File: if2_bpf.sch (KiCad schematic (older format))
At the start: 16 parts

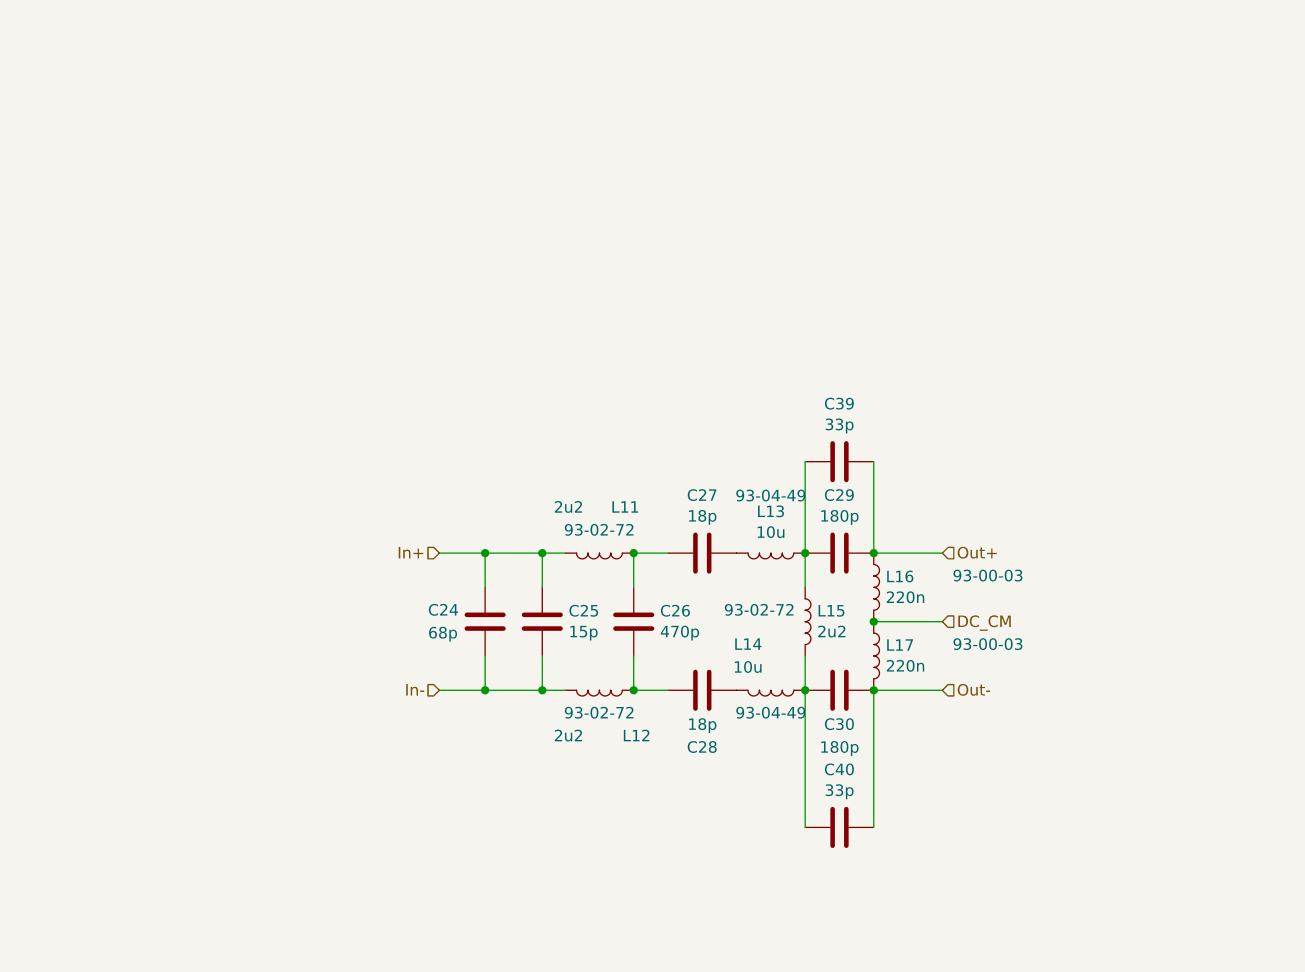
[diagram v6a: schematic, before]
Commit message: if2_bpf revised + Schematic cleanup
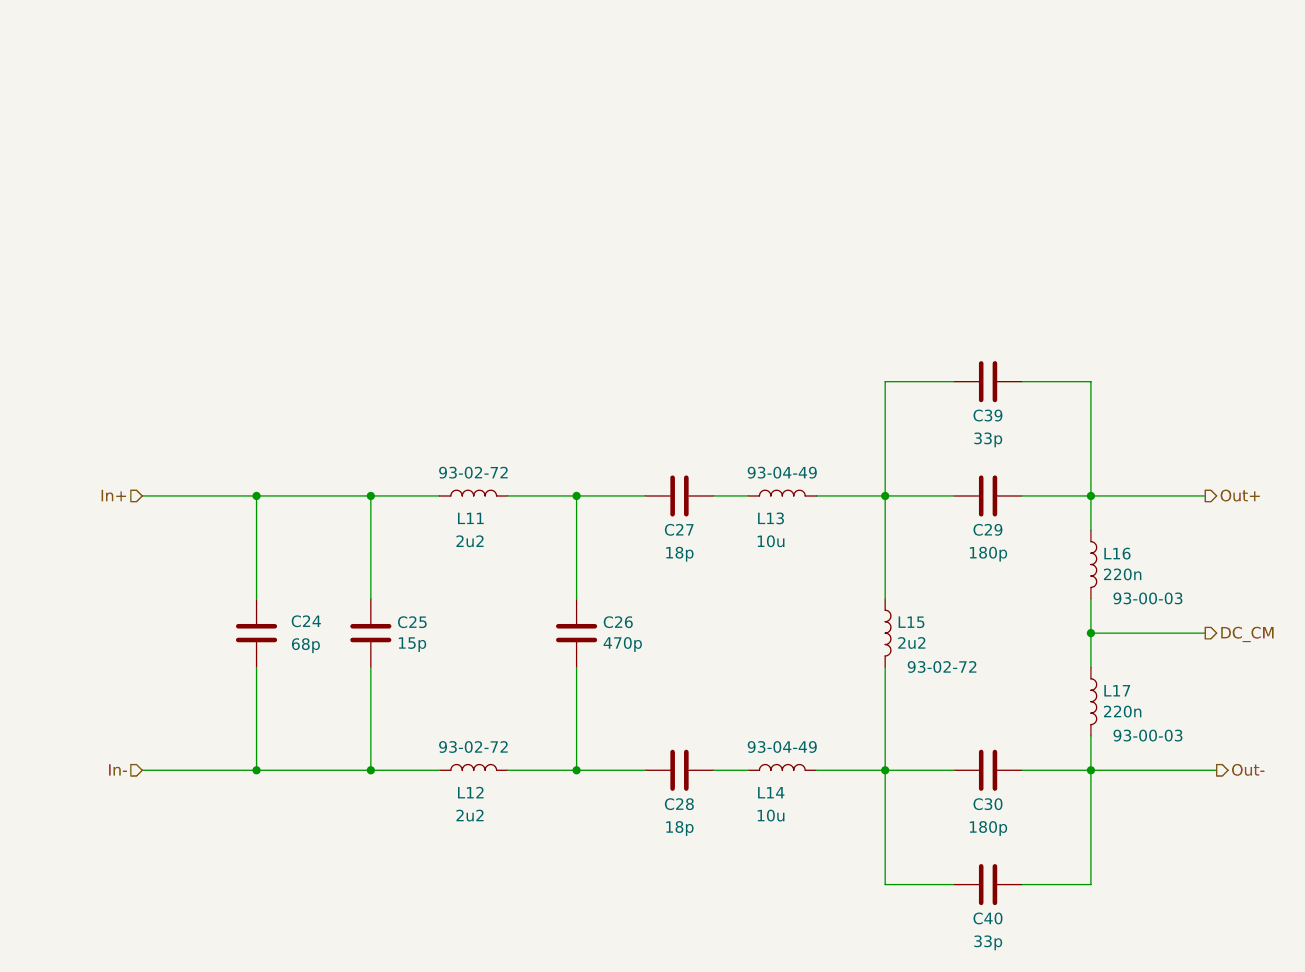
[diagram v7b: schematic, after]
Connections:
- net In+: now also L11.1; no longer L11.2
- net In-: now also L12.1; no longer L12.2
- net Out-: now also C40.2; no longer C40.1
- net at C27.1: now also L13.1; no longer L13.2
- net at C26.1, C27.2: now also L11.2; no longer L11.1
- net at C29.2, C39.2, L15.1: now also L13.2; no longer L13.1
- net at C30.1, L15.2: now also C40.1, L14.2; no longer C40.2, L14.1
- net at C28.1: now also L14.1; no longer L14.2
- net at C26.2, C28.2: now also L12.2; no longer L12.1
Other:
- moved on the sheet: C24, C25, C26, C27, C28, C29, C30, C39, C40, L11, L12, L13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

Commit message: Pcb vHA8KDA
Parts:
- C24, C25, C26, C27, C28, C29, C30, C39, C40: footprint Capacitor_SMD:C_0805_2012Metric_Pad1.15x1.40mm_HandSolder -> Capacitor_SMD:C_0805_2012Metric_Pad1.18x1.45mm_HandSolder
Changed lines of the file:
@@
 F 0 "C24" H 4250 4000 50  0000 L CNN
 F 1 "68p" H 4250 3900 50  0000 L CNN
-F 2 "Capacitor_SMD:C_0805_2012Metric_Pad1.15x1.40mm_HandSolder" H 4138 3800 50  0001 C CNN
+F 2 "Capacitor_SMD:C_0805_2012Metric_Pad1.18x1.45mm_HandSolder" H 4138 3800 50  0001 C CNN
 F 3 "~" H 4100 3950 50  0001 C CNN
 	1    4100 3950
@@
 F 0 "C25" H 4715 3996 50  0000 L CNN
 F 1 "15p" H 4715 3905 50  0000 L CNN
-F 2 "Capacitor_SMD:C_0805_2012Metric_Pad1.15x1.40mm_HandSolder" H 4638 3800 50  0001 C CNN
+F 2 "Capacitor_SMD:C_0805_2012Metric_Pad1.18x1.45mm_HandSolder" H 4638 3800 50  0001 C CNN
 F 3 "~" H 4600 3950 50  0001 C CNN
 	1    4600 3950
@@
 F 0 "C27" V 6100 3350 50  0000 C CNN
 F 1 "18p" V 6200 3350 50  0000 C CNN
-F 2 "Capacitor_SMD:C_0805_2012Metric_Pad1.15x1.40mm_HandSolder" H 5988 3200 50  0001 C CNN
+F 2 "Capacitor_SMD:C_0805_2012Metric_Pad1.18x1.45mm_HandSolder" H 5988 3200 50  0001 C CNN
 F 3 "~" H 5950 3350 50  0001 C CNN
 	1    5950 3350
@@
 F 0 "C29" V 7450 3350 50  0000 C CNN
 F 1 "180p" V 7550 3350 50  0000 C CNN
-F 2 "Capacitor_SMD:C_0805_2012Metric_Pad1.15x1.40mm_HandSolder" H 7338 3200 50  0001 C CNN
+F 2 "Capacitor_SMD:C_0805_2012Metric_Pad1.18x1.45mm_HandSolder" H 7338 3200 50  0001 C CNN
 F 3 "~" H 7300 3350 50  0001 C CNN
 	1    7300 3350
@@
 F 0 "C30" V 7150 4550 50  0000 C CNN
 F 1 "180p" V 7050 4550 50  0000 C CNN
-F 2 "Capacitor_SMD:C_0805_2012Metric_Pad1.15x1.40mm_HandSolder" H 7338 4400 50  0001 C CNN
+F 2 "Capacitor_SMD:C_0805_2012Metric_Pad1.18x1.45mm_HandSolder" H 7338 4400 50  0001 C CNN
 F 3 "~" H 7300 4550 50  0001 C CNN
 	1    7300 4550
@@
 F 0 "C28" V 6100 4550 50  0000 C CNN
 F 1 "18p" V 6200 4550 50  0000 C CNN
-F 2 "Capacitor_SMD:C_0805_2012Metric_Pad1.15x1.40mm_HandSolder" H 5988 4400 50  0001 C CNN
+F 2 "Capacitor_SMD:C_0805_2012Metric_Pad1.18x1.45mm_HandSolder" H 5988 4400 50  0001 C CNN
 F 3 "~" H 5950 4550 50  0001 C CNN
 	1    5950 4550
@@
 F 0 "C26" H 5615 3996 50  0000 L CNN
 F 1 "470p" H 5615 3905 50  0000 L CNN
-F 2 "Capacitor_SMD:C_0805_2012Metric_Pad1.15x1.40mm_HandSolder" H 5538 3800 50  0001 C CNN
+F 2 "Capacitor_SMD:C_0805_2012Metric_Pad1.18x1.45mm_HandSolder" H 5538 3800 50  0001 C CNN
 F 3 "~" H 5500 3950 50  0001 C CNN
 	1    5500 3950
@@
 F 0 "C39" V 7450 2850 50  0000 C CNN
 F 1 "33p" V 7550 2850 50  0000 C CNN
-F 2 "Capacitor_SMD:C_0805_2012Metric_Pad1.15x1.40mm_HandSolder" H 7338 2700 50  0001 C CNN
+F 2 "Capacitor_SMD:C_0805_2012Metric_Pad1.18x1.45mm_HandSolder" H 7338 2700 50  0001 C CNN
 F 3 "~" H 7300 2850 50  0001 C CNN
 	1    7300 2850
@@
 F 0 "C40" V 7150 5050 50  0000 C CNN
 F 1 "33p" V 7050 5050 50  0000 C CNN
-F 2 "Capacitor_SMD:C_0805_2012Metric_Pad1.15x1.40mm_HandSolder" H 7338 4900 50  0001 C CNN
+F 2 "Capacitor_SMD:C_0805_2012Metric_Pad1.18x1.45mm_HandSolder" H 7338 4900 50  0001 C CNN
 F 3 "~" H 7300 5050 50  0001 C CNN
 	1    7300 5050
